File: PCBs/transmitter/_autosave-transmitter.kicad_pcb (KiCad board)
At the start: 4 copper layers, 34 x 70 mm, 72 parts, among them J1 Conn_01x02, J10 1054550101, J11 LoRa, J2 GPIO, J3 Ethernet, J4 Thermistor (10K), J5 RF24, J6 SWD, J7 I2C, J8 Serial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

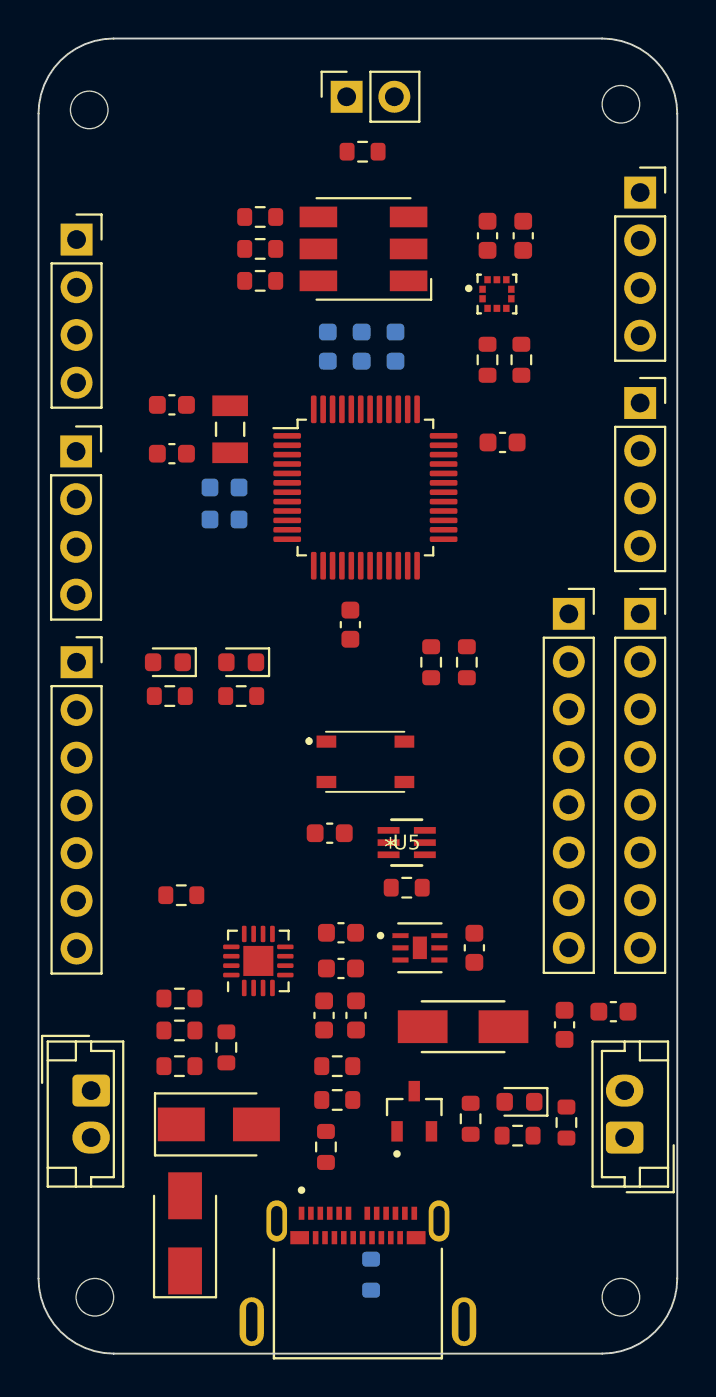
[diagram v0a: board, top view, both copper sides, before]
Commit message: updated schematics
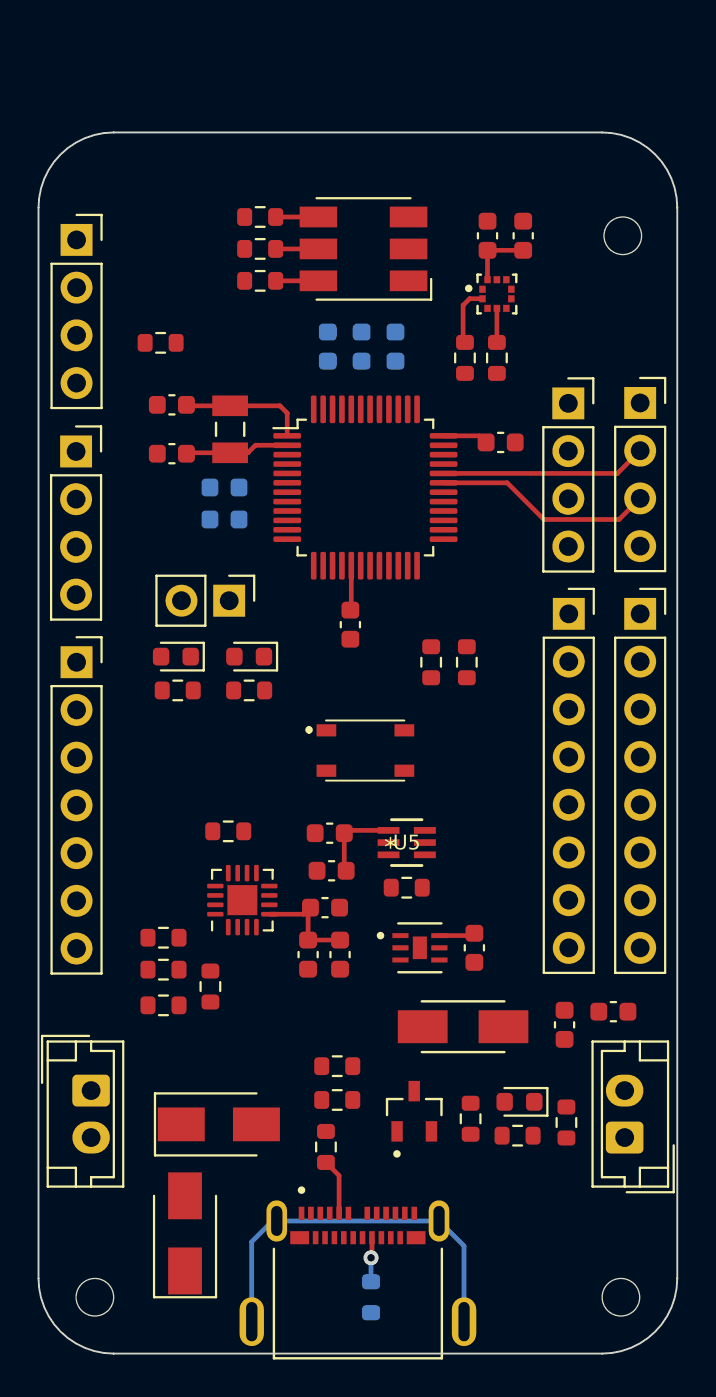
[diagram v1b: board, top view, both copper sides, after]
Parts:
- removed H2: MountingHole, MountingHole:MountingHole_2mm
- J4: footprint Connector_PinSocket_2.54mm:PinSocket_1x02_P2.54mm_Vertical -> Connector_PinHeader_2.54mm:PinHeader_1x02_P2.54mm_Vertical
- moved J4 27.5 mm to (142.2, 98.9), turned to -90 degrees
- moved R6 14.8 mm to (138.5, 85.2)
- moved J6 11.9 mm to (160.2, 88.4)
- moved H3 7.00 mm to (163.1, 79.5)
- moved R11 4.22 mm to (142.1, 111.2)
- moved C12 3.35 mm to (146.3, 117.8)
- moved C13 3.35 mm to (148.1, 117.8)
- moved C14 3.35 mm to (147.2, 115.3)
- moved R10 3.35 mm to (141.2, 119.5)
- moved R12 3.35 mm to (138.7, 118.6)
- moved R13 3.35 mm to (138.7, 120.5)
- moved R9 3.35 mm to (138.7, 116.9)
- moved U2 3.35 mm to (142.8, 114.9)
- moved C16 3.34 mm to (147.6, 113.3)
- moved R4 3.00 mm to (154.7, 86.0)
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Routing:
- net unconnected-(J10-PadS1): track 0.00 -> 20.6 mm
- net /SCL: track 0.00 -> 14.2 mm
- net /SDA: track 0.00 -> 13.5 mm
- net +3V3: track 0.00 -> 13.1 mm
- net Net-(C1-Pad2): track 0.00 -> 6.76 mm
- net /LiPo/SOUT: track 0.00 -> 5.81 mm
- net Net-(C2-Pad2): track 0.00 -> 5.55 mm
- net Net-(J10-PadA5): track 0.00 -> 2.99 mm
- net Net-(J10-PadB5): track 0.00 -> 2.37 mm, vias 0 -> 1
- net Net-(D7-Pad6): track 0.00 -> 2.28 mm
- net Net-(D7-Pad5): track 0.00 -> 2.28 mm
- net Net-(D7-Pad4): track 0.00 -> 2.28 mm
- net /Regulators/+5V_reg: track 0.00 -> 1.92 mm
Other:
- board size 34 x 70 mm -> 34 x 65 mm
